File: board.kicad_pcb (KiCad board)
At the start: 4 copper layers, 72 x 46.5 mm, 49 parts, among them J1 H3, J2 USB-UART, J3 H2, J4 H1, J5 PWR, J6 DL, J7 H4, Q1 Q_NPN_BCE, Q2 Q_NPN_BCE, SW1 RESET, U1 ASSoC, U2 LM1117-3.3, U3 LM1117-3.3, Y1 25 MHz

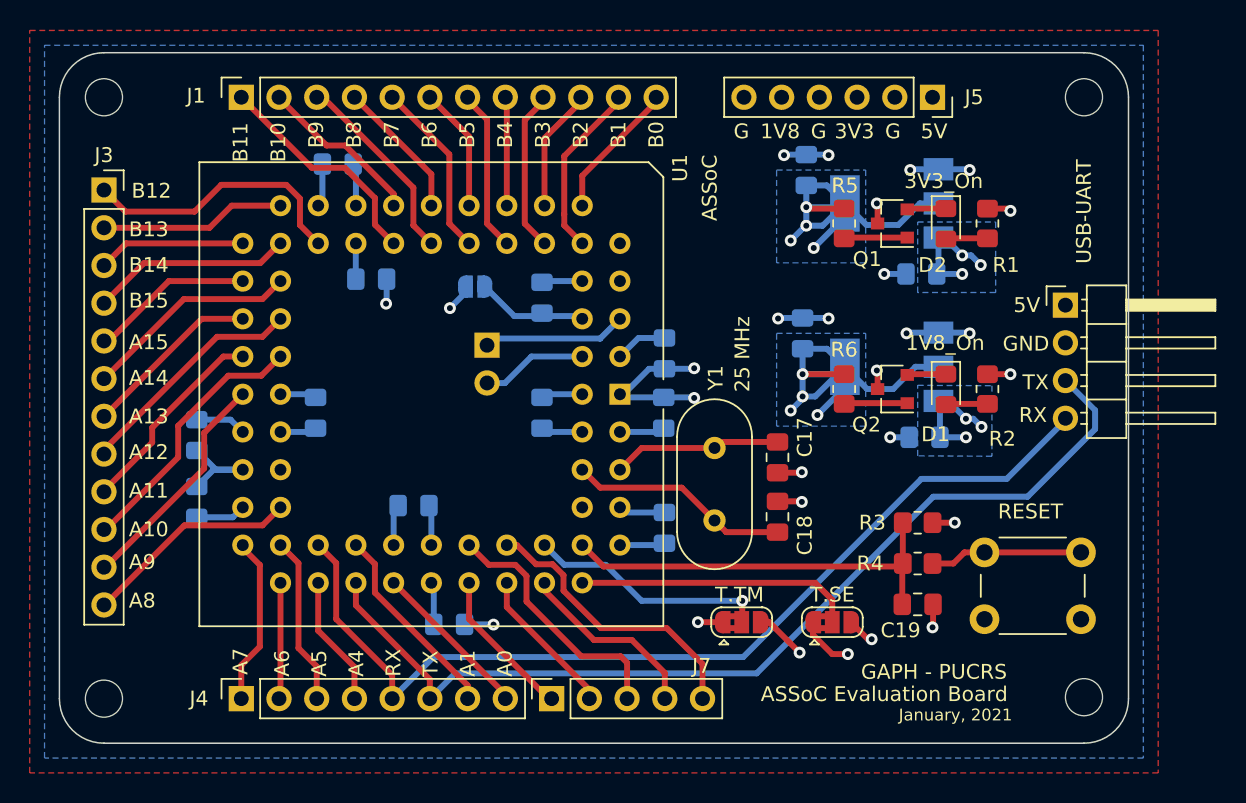
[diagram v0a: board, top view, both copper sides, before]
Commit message: Update copper areas
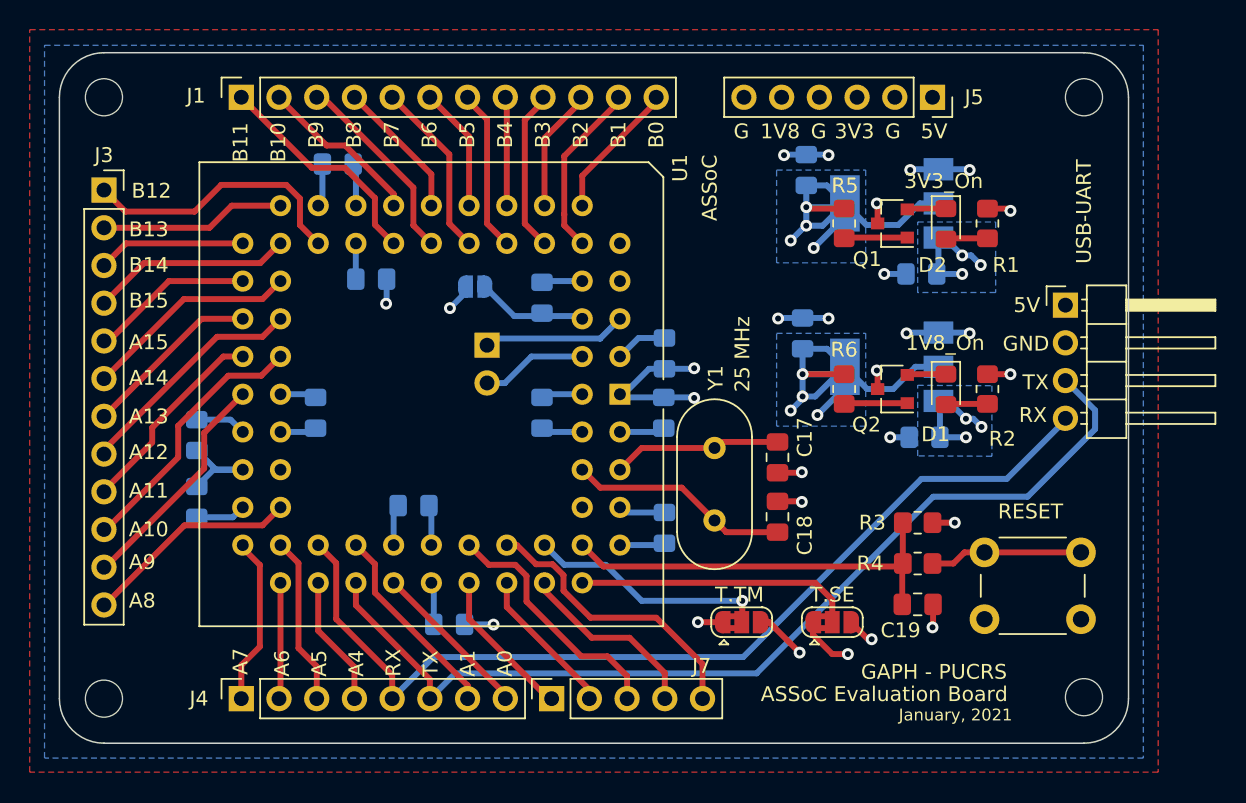
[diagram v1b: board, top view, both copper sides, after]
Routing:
- net /M.MOSI: track 17.3 -> 16.8 mm
- removed copper zone on B.Cu, net (none)
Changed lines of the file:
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@@
     (user_trace_width 0.6)
     (trace_clearance 0.3)
-    (zone_clearance 0.508)
+    (zone_clearance 0.4)
     (zone_45_only no)
     (trace_min 0.2)
@@
       (padsonsilk false)
       (subtractmaskfromsilk false)
-      (outputformat 4)
+      (outputformat 1)
       (mirror false)
       (drillshape 0)
@@
   (segment (start 169.95 111.15) (end 169.2 111.9) (width 0.4) (layer F.Cu) (net 51))
   (segment (start 171.3 111.15) (end 169.95 111.15) (width 0.4) (layer F.Cu) (net 51))
-  (segment (start 147.55 117.05) (end 149.77 119.27) (width 0.4) (layer F.Cu) (net 52))
-  (segment (start 145 117.05) (end 147.55 117.05) (width 0.4) (layer F.Cu) (net 52))
   (segment (start 149.77 119.27) (end 149.77 121) (width 0.4) (layer F.Cu) (net 52))
-  (segment (start 141.67 113.72) (end 145 117.05) (width 0.4) (layer F.Cu) (net 52))
+  (segment (start 147.4 116.9) (end 149.77 119.27) (width 0.4) (layer F.Cu) (net 52))
+  (segment (start 144.85 116.9) (end 147.4 116.9) (width 0.4) (layer F.Cu) (net 52))
+  (segment (start 141.67 113.72) (end 144.85 116.9) (width 0.4) (layer F.Cu) (net 52))
   (segment (start 141.67 113.2) (end 141.67 113.72) (width 0.4) (layer F.Cu) (net 52))
   (segment (start 141.95 121) (end 142.15 121) (width 0.4) (layer F.Cu) (net 53))
   (segment (start 136.59 115.64) (end 141.95 121) (width 0.4) (layer F.Cu) (net 53))
   (segment (start 136.59 113.2) (end 136.59 115.64) (width 0.4) (layer F.Cu) (net 53))
-  (segment (start 147.23 118.58) (end 147.23 121) (width 0.4) (layer F.Cu) (net 54))
-  (segment (start 146.8 118.15) (end 147.23 118.58) (width 0.4) (layer F.Cu) (net 54))
-  (segment (start 144.15 118.15) (end 146.8 118.15) (width 0.4) (layer F.Cu) (net 54))
-  (segment (start 139.711377 111.988799) (end 140.458799 112.736221) (width 0.4) (layer F.Cu) (net 54))
+  (segment (start 147.23 119.48) (end 147.23 121) (width 0.4) (layer F.Cu) (net 54))
+  (segment (start 145.9 118.15) (end 147.23 119.48) (width 0.4) (layer F.Cu) (net 54))
+  (segment (start 144.15 118.15) (end 145.9 118.15) (width 0.4) (layer F.Cu) (net 54))
   (segment (start 140.458799 114.458799) (end 144.15 118.15) (width 0.4) (layer F.Cu) (net 54))
-  (segment (start 137.918799 111.988799) (end 139.711377 111.988799) (width 0.4) (layer F.Cu) (net 54))
   (segment (start 140.458799 112.736221) (end 140.458799 114.458799) (width 0.4) (layer F.Cu) (net 54))
+  (segment (start 139.711377 111.988799) (end 140.458799 112.736221) (width 0.4) (layer F.Cu) (net 54))
+  (segment (start 137.918799 111.988799) (end 139.711377 111.988799) (width 0.4) (layer F.Cu) (net 54))
   (segment (start 136.59 110.66) (end 137.918799 111.988799) (width 0.4) (layer F.Cu) (net 54))
   (segment (start 144.69 120.39) (end 144.69 121) (width 0.4) (layer F.Cu) (net 55))
@@
   (segment (start 139.13 110.66) (end 139.13 110.77) (width 0.4) (layer F.Cu) (net 56))
   (segment (start 152.31 118.66) (end 152.31 121) (width 0.4) (layer F.Cu) (net 56))
-  (segment (start 145.467422 116.25) (end 149.9 116.25) (width 0.4) (layer F.Cu) (net 56))
-  (segment (start 142.95 112.687422) (end 142.95 113.732578) (width 0.4) (layer F.Cu) (net 56))
-  (segment (start 142.95 113.732578) (end 145.467422 116.25) (width 0.4) (layer F.Cu) (net 56))
-  (segment (start 141.1 111.95) (end 142.212578 111.95) (width 0.4) (layer F.Cu) (net 56))
+  (segment (start 149.2 115.55) (end 152.31 118.66) (width 0.4) (layer F.Cu) (net 56))
+  (segment (start 144.767422 115.55) (end 149.2 115.55) (width 0.4) (layer F.Cu) (net 56))
   (segment (start 142.212578 111.95) (end 142.95 112.687422) (width 0.4) (layer F.Cu) (net 56))
+  (segment (start 141.1 111.95) (end 142.212578 111.95) (width 0.4) (layer F.Cu) (net 56))
+  (segment (start 142.95 112.687422) (end 142.95 113.732578) (width 0.4) (layer F.Cu) (net 56))
   (segment (start 139.81 110.66) (end 141.1 111.95) (width 0.4) (layer F.Cu) (net 56))
-  (segment (start 149.9 116.25) (end 152.31 118.66) (width 0.4) (layer F.Cu) (net 56))
+  (segment (start 142.95 113.732578) (end 144.767422 115.55) (width 0.4) (layer F.Cu) (net 56))
   (segment (start 139.13 110.66) (end 139.81 110.66) (width 0.4) (layer F.Cu) (net 56))
   (zone (net 1) (net_name GND) (layer B.Cu) (hatch edge 0.508)
-    (connect_pads (clearance 0.508))
-    (min_thickness 0.254)
-    (fill yes (arc_segments 32) (thermal_gap 0.508) (thermal_bridge_width 0.508) (smoothing chamfer) (radius 1))
+    (connect_pads (clearance 0.4))
+    (min_thickness 0.38)
+    (fill yes (arc_segments 32) (thermal_gap 0.4) (thermal_bridge_width 0.4) (smoothing chamfer) (radius 1))
     (polygon
       (pts
@@
   )
   (zone (net 1) (net_name GND) (layer F.Cu) (hatch edge 0.508)
-    (connect_pads (clearance 0.508))
-    (min_thickness 0.254)
-    (fill yes (arc_segments 32) (thermal_gap 0.508) (thermal_bridge_width 0.508))
+    (connect_pads (clearance 0.4))
+    (min_thickness 0.38)
+    (fill yes (arc_segments 32) (thermal_gap 0.4) (thermal_bridge_width 0.4) (smoothing fillet) (radius 2))
     (polygon
       (pts
-        (xy 183 126) (xy 107 126) (xy 107 76) (xy 183 76)
+        (xy 183 125.95) (xy 107 125.95) (xy 107 75.95) (xy 183 75.95)
       )
     )
@@
     (connect_pads (clearance 0.508))
     (min_thickness 0.254)
-    (fill yes (arc_segments 32) (thermal_gap 0.508) (thermal_bridge_width 0.508) (smoothing fillet))
+    (fill yes (arc_segments 32) (thermal_gap 0.508) (thermal_bridge_width 0.508) (smoothing fillet) (radius 2))
     (polygon
       (pts
@@
     (connect_pads (clearance 0.508))
     (min_thickness 0.254)
-    (fill yes (arc_segments 32) (thermal_gap 0.508) (thermal_bridge_width 0.508) (smoothing fillet))
+    (fill yes (arc_segments 32) (thermal_gap 0.508) (thermal_bridge_width 0.508) (smoothing fillet) (radius 2))
     (polygon
       (pts
@@
   (zone (net 7) (net_name +5V) (layer B.Cu) (hatch edge 0.508)
     (priority 1)
-    (connect_pads (clearance 0.508))
-    (min_thickness 0.254)
-    (fill yes (arc_segments 32) (thermal_gap 0.508) (thermal_bridge_width 0.508) (smoothing fillet))
+    (connect_pads (clearance 0.4))
+    (min_thickness 0.38)
+    (fill yes (arc_segments 32) (thermal_gap 0.4) (thermal_bridge_width 0.4) (smoothing fillet) (radius 2))
     (polygon
       (pts
@@
     )
   )
-  (zone (net 0) (net_name "") (layer B.Cu) (hatch edge 0.508)
+  (zone (net 7) (net_name +5V) (layer B.Cu) (hatch edge 0.508)
     (priority 1)
-    (connect_pads (clearance 0.508))
-    (min_thickness 0.254)
-    (fill yes (arc_segments 32) (thermal_gap 0.508) (thermal_bridge_width 0.508) (smoothing fillet))
+    (connect_pads (clearance 0.4))
+    (min_thickness 0.38)
+    (fill yes (arc_segments 32) (thermal_gap 0.4) (thermal_bridge_width 0.4) (smoothing fillet) (radius 2))
     (polygon
       (pts
